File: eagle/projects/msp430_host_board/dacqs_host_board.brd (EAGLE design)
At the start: 127 x 102 mm, 181 parts, among them J1 MOL-SL-4-RA, J10 MOL-SL-3-V, J13 JST-PH-2TH-RA, J14 USB_MICROB_RECPT, J16 MOL-SL-2-RA, J17 CLM-112-02-L-D-IMU-MOUNT_IMU, J18 MOLSL-7-RA, J2 MOL-SL-4-RA, J3 MOL-SL-4-RA, J4 MOL-SL-4-RA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

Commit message: Started power layout
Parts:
- moved BAT1 72.0 mm to (116.0, 25.8)
- moved C14 43.9 mm to (29.4, 85.7), turned to 180 degrees
- moved TP35 42.8 mm to (22.6, 33.5)
- moved C21 37.9 mm to (30.4, 42.6)
- moved C5 34.7 mm to (26.8, 27.8)
- moved U8 32.8 mm to (16.7, 33.3)
- moved U3 31.0 mm to (34.5, 29.7)
- moved R1 29.9 mm to (53.0, 84.6)
- moved U10 29.9 mm to (47.9, 49.8)
- moved DS1 29.3 mm to (20.5, 56.1), turned to 180 degrees
- moved R12 28.8 mm to (26.6, 30.0)
- moved Y3 28.6 mm to (34.0, 85.8)
- moved R27 27.2 mm to (58.9, 46.8)
- moved C10 26.2 mm to (29.3, 63.6)
- moved C9 26.0 mm to (29.2, 67.4)
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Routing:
- net GND: track 444.7 -> 0.00 mm, vias 3 -> 0
- net +3V3: track 211.4 -> 17.7 mm, vias 9 -> 0
- net SENSE_SCL_1: track 162.8 -> 0.00 mm, vias 5 -> 0
- net SENSE_SDA_1: track 159.1 -> 0.00 mm, vias 5 -> 0
- net RST_SBWTDIO_MOTOR: track 157.0 -> 0.00 mm, vias 4 -> 0
- net +5V: track 158.0 -> 3.42 mm, vias 5 -> 0
- net SENSE_SCL_2: track 142.4 -> 0.00 mm, vias 2 -> 0
- net CUTDOWN_EN: track 129.7 -> 0.00 mm, vias 5 -> 0
- net SENSE_SDA_2: track 116.7 -> 0.00 mm, vias 4 -> 0
- net SBWTCK_HOST: track 112.5 -> 0.00 mm, vias 1 -> 0
- net VBAT_POS: track 112.1 -> 0.00 mm
- net SD_CS: track 105.4 -> 0.00 mm, vias 2 -> 0
- net RST_SBWTDIO_HOST: track 102.2 -> 0.00 mm
- net UART_4_TX: track 99.6 -> 0.00 mm, vias 3 -> 0
- net RST_PI_3: track 96.3 -> 0.00 mm, vias 4 -> 0
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
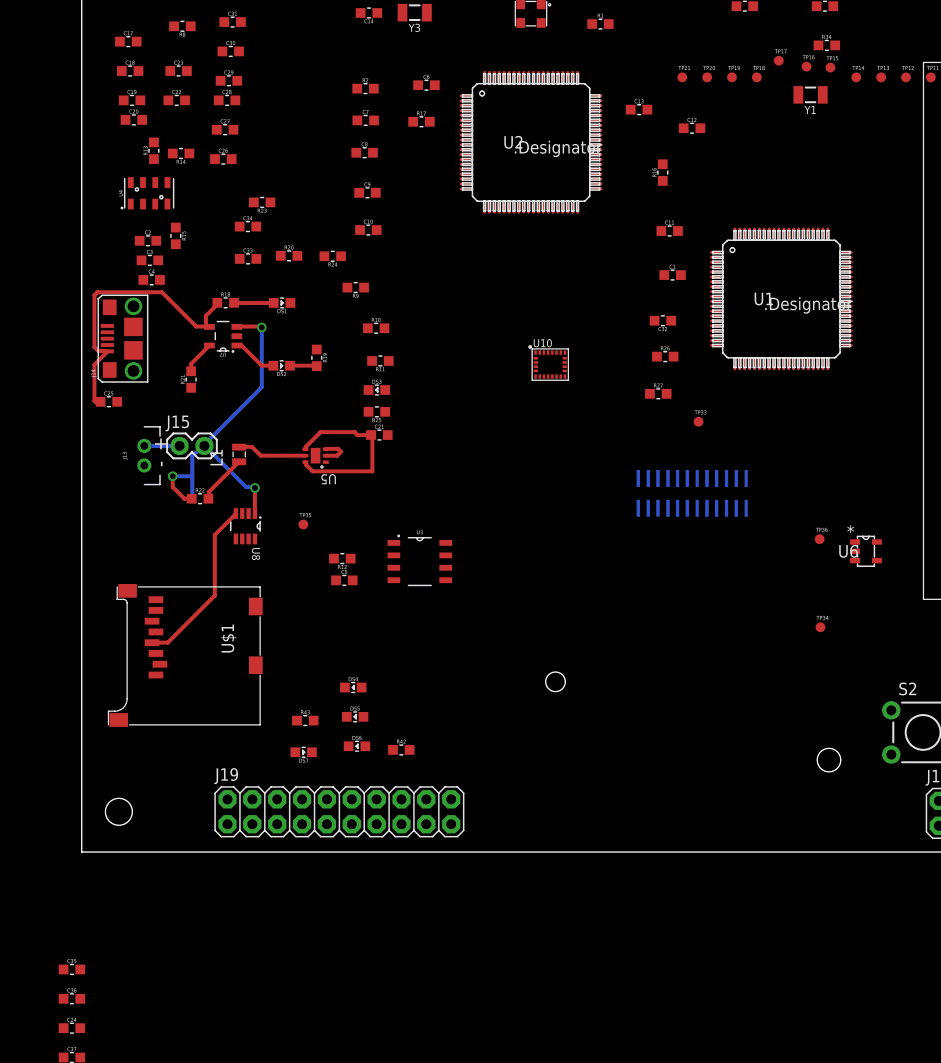
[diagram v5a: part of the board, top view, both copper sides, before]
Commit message: Work on the power management placement and routing. Also added new schematic pdfs
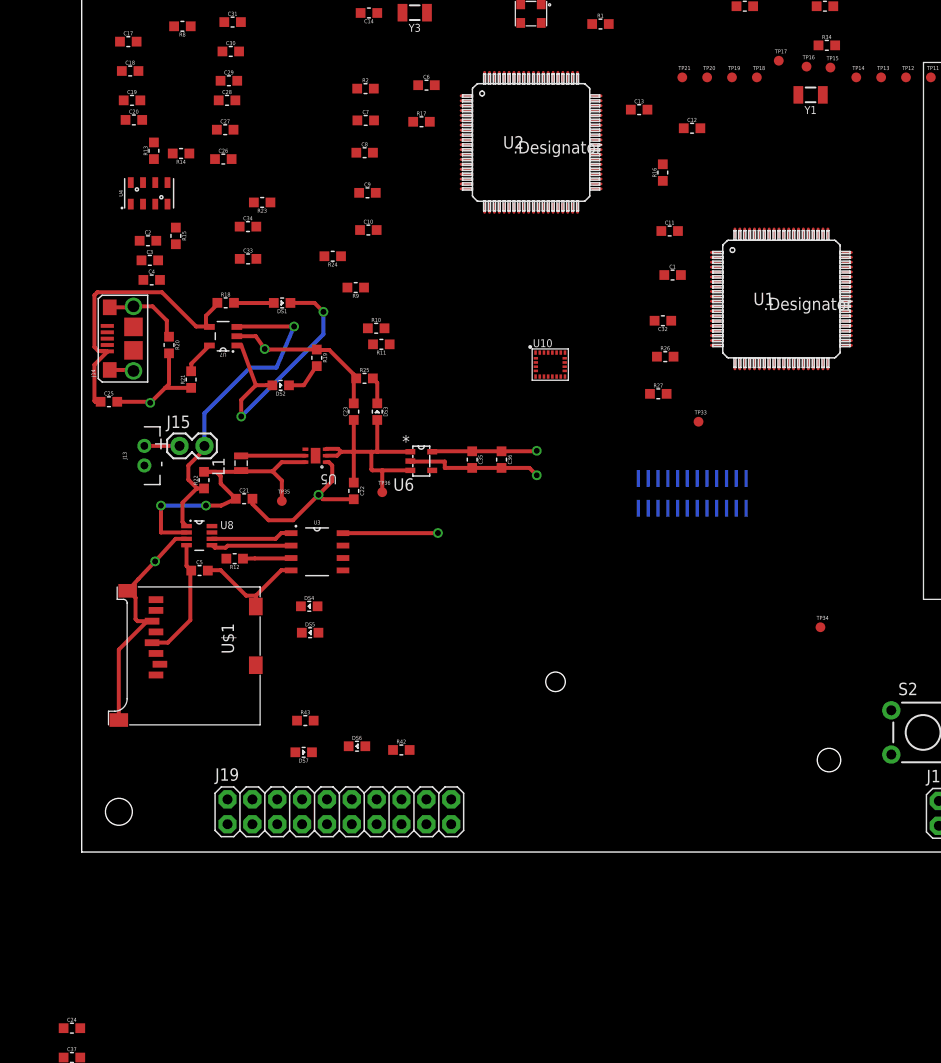
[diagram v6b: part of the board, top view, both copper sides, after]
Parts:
- moved C36 70.5 mm to (42.9, 40.1), turned to 270 degrees
- moved C35 66.2 mm to (39.9, 40.1), turned to 270 degrees
- moved U6 46.4 mm to (34.7, 40.0)
- moved TP36 45.0 mm to (30.7, 36.8)
- moved C22 43.8 mm to (27.8, 36.9), turned to 270 degrees
- moved C23 39.1 mm to (27.8, 45.0), turned to 90 degrees
- moved R20 15.3 mm to (8.92, 51.8), turned to 270 degrees
- moved C21 15.3 mm to (16.6, 36.1)
- moved C5 14.8 mm to (12.0, 28.8)
- moved R12 11.0 mm to (15.6, 30.0)
- moved U3 10.5 mm to (24.1, 30.7)
- moved DS5 9.75 mm to (23.3, 22.4)
- moved DS4 9.44 mm to (23.2, 25.1)
- moved U8 4.82 mm to (12.0, 32.3), turned to 0 degrees
- moved R25 3.64 mm to (28.9, 48.4), turned to 0 degrees
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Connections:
- net GND: now also R36.2, R37.2, R38.2, R39.2, R40.2, R41.2, TP40.TP
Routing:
- net GND: track 0.00 -> 96.1 mm, vias 0 -> 5
- net +5V: track 3.42 -> 28.2 mm
- net BATT_CHARGE_STAT: track 4.61 -> 28.3 mm, vias 0 -> 2
- net +3V3: track 17.7 -> 33.2 mm, vias 0 -> 2
- net SHIELD_GND: track 0.00 -> 10.7 mm
- net SENSE_SDA_1: track 0.00 -> 8.35 mm
- net SENSE_SCL_1: track 0.00 -> 8.29 mm
- net VBAT_SENSE_N: track 24.1 -> 32.2 mm, vias 0 -> 2
- net OVER_TEMP_SHUTDOWN: track 0.00 -> 4.97 mm
- net VBAT: track 38.3 -> 34.0 mm, vias 3 -> 1
- net LED_BLUE_5V: track 0.00 -> 2.74 mm
- net VBAT_READY: track 2.78 -> 3.96 mm
- net TPS6_L: track 7.15 -> 6.58 mm

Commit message: Worked on power management
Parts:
- removed J15: (no value), daqcs_host:1X02
- added J11: MOL-SL-2-V, daqcs_host:MOLSL-2-V
- moved TP38 30.1 mm to (19.2, 61.2)
- moved U8 26.9 mm to (28.1, 53.8)
- moved C25 18.7 mm to (10.3, 63.1), turned to 270 degrees
- moved R23 15.6 mm to (31.6, 58.0), turned to 270 degrees
- moved R20 14.5 mm to (11.1, 66.1), turned to 0 degrees
- moved U4 12.4 mm to (4.79, 79.5)
- moved C2 12.4 mm to (4.67, 74.7)
- moved C3 12.4 mm to (4.86, 72.7)
- moved C4 12.4 mm to (5.05, 70.7)
- moved R15 12.4 mm to (7.52, 75.2)
- moved C10 11.3 mm to (25.6, 74.3)
- moved C9 11.3 mm to (25.5, 78.1)
- moved R10 11.3 mm to (26.4, 64.2)
- moved R11 11.3 mm to (26.9, 62.6)
- moved R9 11.3 mm to (24.3, 68.4)
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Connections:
- net VBAT: now also J11.1; no longer J15.2
- net VBAT_IN: now also J11.2; no longer J15.1
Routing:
- net VBAT_SENSE_N: track 32.2 -> 46.5 mm, vias 2 -> 0
- net GND: track 96.1 -> 107.8 mm, vias 5 -> 3
- net USB_5V: track 29.8 -> 18.5 mm
- net VBAT: track 34.0 -> 44.9 mm, vias 1 -> 2
- net +3V3: track 33.2 -> 41.7 mm, vias 2 -> 1
- net SENSE_SDA_1: track 8.35 -> 0.00 mm
- net SENSE_SCL_1: track 8.29 -> 0.00 mm
- net VBAT_IN: track 3.60 -> 9.21 mm
- net BATT_CHARGE_STAT: track 28.3 -> 33.8 mm, vias 2 -> 0
- net CURRENT_I2C_A0: track 0.00 -> 4.98 mm
- net +5V: track 28.2 -> 25.2 mm
- net CURRENT_I2C_A1: track 0.00 -> 2.40 mm
- net VBAT_READY: track 3.96 -> 3.11 mm
- net VBAT_CHARGING: track 4.08 -> 3.40 mm

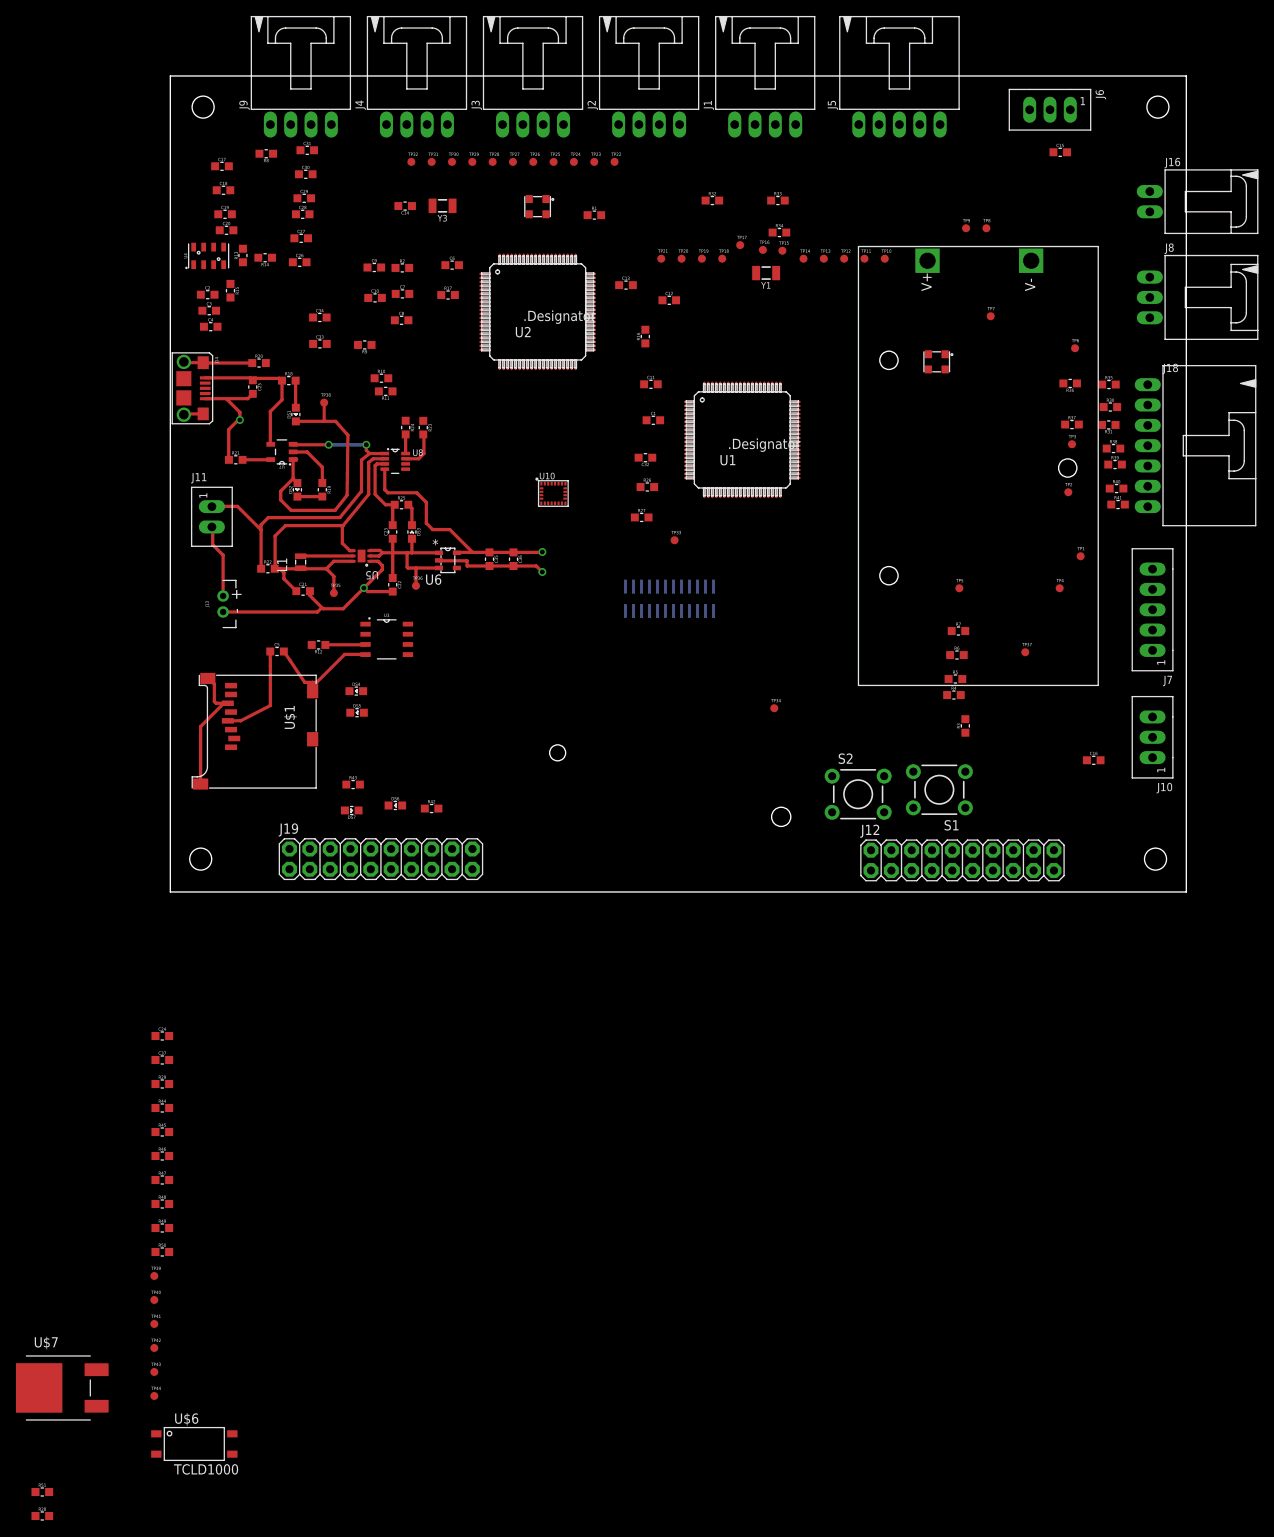
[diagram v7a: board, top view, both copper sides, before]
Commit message: Worked on power layout and tracing to msp430s
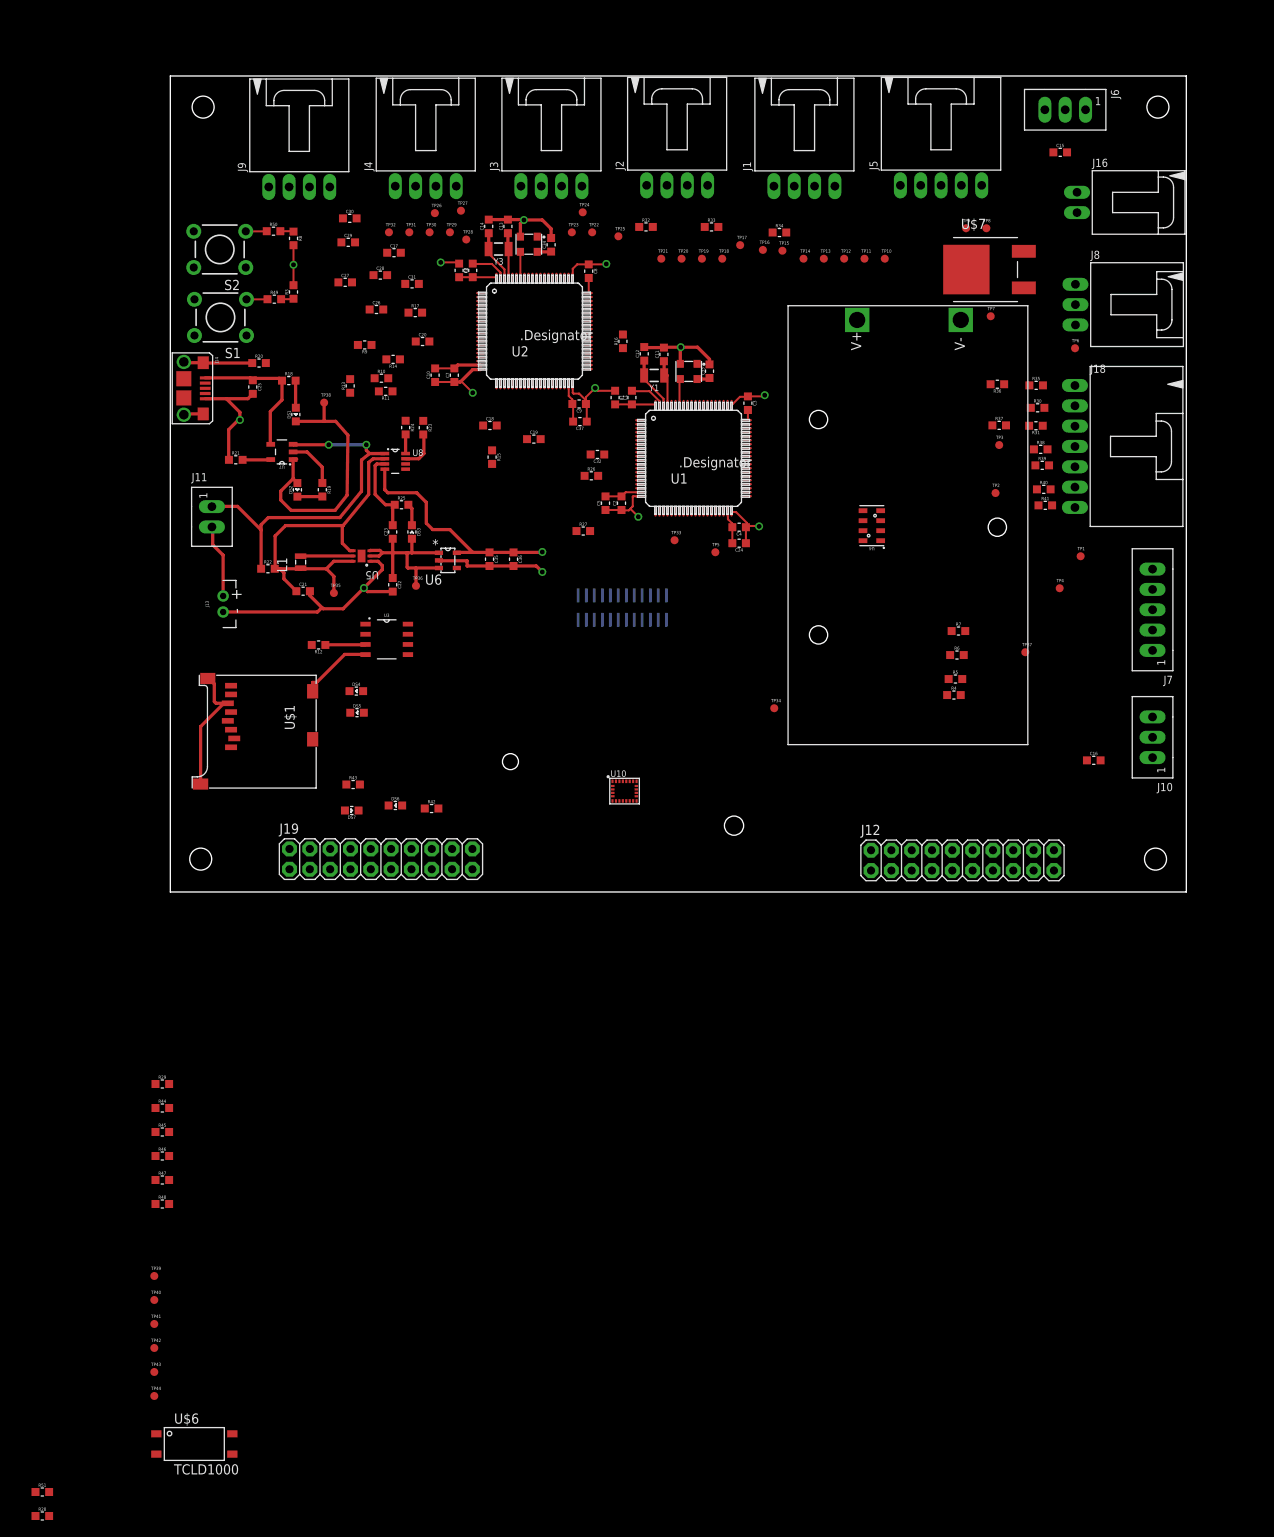
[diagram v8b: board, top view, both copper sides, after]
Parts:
- moved U$7 181.6 mm to (103.9, 77.8)
- moved R50 128.4 mm to (12.9, 82.6)
- moved R49 116.9 mm to (13.0, 74.1)
- moved S1 107.5 mm to (6.27, 71.8)
- moved S2 104.9 mm to (6.18, 80.3), turned to 180 degrees
- moved R3 100.0 mm to (15.4, 75.0)
- moved C37 95.4 mm to (51.2, 58.8), turned to 180 degrees
- moved C24 94.8 mm to (71.1, 43.6), turned to 180 degrees
- moved U4 89.5 mm to (87.7, 45.8), turned to 180 degrees
- moved C4 70.6 mm to (71.1, 45.6), turned to 180 degrees
- moved C3 68.3 mm to (72.2, 61.1), turned to 270 degrees
- moved C2 57.9 mm to (56.4, 48.6), turned to 90 degrees
- moved C33 48.8 mm to (67.4, 65.1), turned to 90 degrees
- moved C19 47.7 mm to (45.4, 56.6)
- moved C5 45.1 mm to (54.4, 48.6), turned to 90 degrees
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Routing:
- net GND: track 107.8 -> 156.9 mm, vias 3 -> 5
- net +3V3: track 41.7 -> 82.7 mm, vias 1 -> 9
- net LF_IN_1: track 0.00 -> 5.85 mm
- net LF_OUT_1: track 0.00 -> 5.75 mm
- net LF_IN_2: track 0.00 -> 5.54 mm
- net LF_OUT_2: track 0.00 -> 5.48 mm
- net AVCC_HOST: track 0.00 -> 5.05 mm
- net AVCC_MOTOR: track 0.00 -> 4.68 mm
- net HF_IN_1: track 0.00 -> 3.28 mm
- net HF_IN_2: track 0.00 -> 3.18 mm
- net RST_S1: track 0.00 -> 2.64 mm
- net RST_S2: track 0.00 -> 2.63 mm
- net RST_SBWTDIO_MOTOR: track 0.00 -> 1.67 mm
- net VBAT_MOD_CELL_6: track 1.60 -> 0.00 mm
- net RST_SBWTDIO_HOST: track 0.00 -> 1.57 mm
